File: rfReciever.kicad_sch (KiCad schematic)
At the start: 27 parts, among them P1 USB_C_Plug_USB2.0, SW1 SW_Push, SW2 SW_Push, U1 XBee_SMT, U2 CP2102N-Axx-xQFN20, U3 USBLC6-2SC6

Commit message: double schematic about to fix
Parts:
- removed U1: XBee_SMT, RF_Module:Digi_XBee_SMT, symbol RF_ZigBee:XBee_SMT
- added C1, C3: 4.7uF, Capacitor_SMD:C_0805_2012Metric, symbol Device:C
- added C2, C4: 0.1uF, Capacitor_SMD:C_0805_2012Metric, symbol Device:C
- added C5: 47pF, Capacitor_SMD:C_0805_2012Metric, symbol Device:C
- added C6: 1uF, Capacitor_SMD:C_0805_2012Metric, symbol Device:C
- added C7: 10uF, Capacitor_SMD:C_0805_2012Metric, symbol Device:C
- added D10, D5, D6, D7, D8, D9: LED, LED_SMD:LED_0805_2012Metric, symbol Device:LED
- added P2: USB_C_Plug_USB2.0, Connector_USB:USB_C_Plug_JAE_DX07P024AJ1, symbol Connector:USB_C_Plug_USB2.0
- added R1, R13, R14, R15, R16, R18, R19: 1K, Resistor_SMD:R_0805_2012Metric, symbol Device:R
- added R11: 10K, Resistor_SMD:R_0805_2012Metric, symbol Device:R
- added R12, R17: 10k, Resistor_SMD:R_0805_2012Metric, symbol Device:R
- added R4: 5.1K, Resistor_SMD:R_0805_2012Metric, symbol Device:R
- added SW3: SW_Push, Button_Switch_THT:SW_PUSH_6mm_H4.3mm, symbol Switch:SW_Push
- added U1: CP2102N-Axx-xQFN20, Audio_Module:QFN24_CP2102N_SIL, symbol Interface_USB:CP2102N-Axx-xQFN20
- added U4: USBLC6-2SC6, Package_TO_SOT_SMD:SOT-23-6, symbol Power_Protection:USBLC6-2SC6
- added X1, X2: DigiXBeeRX900Micro, symbol DataAcqLeaderBoard-Symbols:DigiXBeeRX900Micro
- C1, C3, C5: footprint Capacitor_SMD:C_0603_1608Metric_Pad1.08x0.95mm_HandSolder -> Capacitor_SMD:C_0805_2012Metric
- C2: footprint Capacitor_SMD:C_01005_0402Metric_Pad0.57x0.30mm_HandSolder -> Capacitor_SMD:C_0805_2012Metric
- C4, C6: footprint Capacitor_SMD:C_0402_1005Metric_Pad0.74x0.62mm_HandSolder -> Capacitor_SMD:C_0805_2012Metric
- C7: footprint Capacitor_SMD:C_0805_2012Metric_Pad1.18x1.45mm_HandSolder -> Capacitor_SMD:C_0805_2012Metric
- D1, D4: footprint LED_SMD:LED_0201_0603Metric -> LED_SMD:LED_0805_2012Metric
- D2, D3: footprint LED_SMD:LED_0603_1608Metric_Pad1.05x0.95mm_HandSolder -> LED_SMD:LED_0805_2012Metric
- R1, R10, R2, R3, R4, R9: footprint Resistor_SMD:R_0603_1608Metric_Pad0.98x0.95mm_HandSolder -> Resistor_SMD:R_0805_2012Metric
- R5, R8: value 330 -> 1K; footprint Resistor_SMD:R_0603_1608Metric_Pad0.98x0.95mm_HandSolder -> Resistor_SMD:R_0805_2012Metric
- R6, R7: value 220 -> 1K; footprint Resistor_SMD:R_0603_1608Metric_Pad0.98x0.95mm_HandSolder -> Resistor_SMD:R_0805_2012Metric
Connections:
- net 3.3V (out): now also X1.14 (SPI_N_SSEL/DIO17), X1.2 (VCC)
- net 5V(in): no longer R3.1
- net GND: now also C1.2, C2.2, C3.1, C4.1, C5.2, C6.2, C7.2, D10.1 (K), D5.1 (K), D6.1 (K), D7.1 (K), D8.1 (K), D9.1 (K), P2.A1 (GND), P2.A12 (GND), P2.B1 (GND), P2.B12 (GND), P2.S1 (SHIELD), R4.2, SW3.1, U1.12 (GND), U1.21 (GND), U1.3 (GND), U4.2 (GND), X1.1 (GND), X1.10 (GND), X1.12 (GND), X1.21 (GND), X1.32 (GND), X1.34 (GND), X2.1 (GND), X2.10 (GND), X2.12 (GND), X2.21 (GND), X2.32 (GND), X2.34 (GND)
- net at R2.1, R3.2: now also U1.8 (VBUS); no longer U2.8 (VBUS)
- net at R7.1, U2.18 (TXD): now also X1.4 (UART_RX/N_CONFIG/DIO14)
- net at R6.1, U2.17 (RXD): now also X1.3 (UART_TX/DIO13)
- net at R8.1: now also X1.7 (RSSI/PWM/DIO10)
- net at R5.1: now also X1.26 (ASSOCIATE/DIO5)
- net at U2.16 (~{RTS}): now also X1.24 (N_CTS/DIO7)
- net at U2.15 (~{CTS}): now also X1.27 (N_RTS/DIO6)
- new net: D6.2 (A), R14.2
- new net: C3.2, C4.2, R1.2, U1.6 (VDD)
- new net: P2.A5 (CC), R4.1
- new net: R19.1, X2.15 (ASSOCIATE/SPI_MOSI/DIO16)
- new net: D10.2 (A), R19.2
- new net: R12.2, SW3.2, X2.6 (N_RESET)
- new net: R11.2, X2.14 (SPI_N_SSEL/DIO17)
- new net: D5.2 (A), R13.2
- new net: R16.1, X2.25 (ON/N_SLEEP/DIO9)
- new net: R18.1, X2.26 (ASSOCIATE/DIO5)
- new net: R15.1, X2.7 (RSSI/PWM/DIO10)
- new net: D7.2 (A), R15.2
- new net: D8.2 (A), R16.2
- new net: D9.2 (A), R18.2
- new net: P2.A6 (D+), U4.3 (I/O2)
- new net: P2.A7 (D-), U4.1 (I/O1)
- new net: U1.4 (D+), U4.4 (I/O2)
- new net: U1.5 (D-), U4.6 (I/O1)
- new net 3.3V: C5.1, C6.1, C7.1, R1.1, R11.1, R12.1, R17.1, U1.9 (~{RST}), X2.2 (VCC)
- new net CTS(Bridge): U1.15 (~{CTS}), X2.27 (N_RTS/DIO6)
- new net RF_BOOTMODE: R17.2, X2.11 (N_BOOTMODE/SPI_N_ATTN/DIO19)
- new net RF_SLEEP: X2.9 (N_DTR/SLEEP_RQ/DIO8)
- new net RTS(Bridge): U1.16 (~{RTS}), X2.24 (N_CTS/DIO7)
- new net RXD(Bridge): R14.1, U1.17 (RXD), X2.3 (UART_TX/DIO13)
- new net TXD(Bridge): R13.1, U1.18 (TXD), X2.4 (UART_RX/N_CONFIG/DIO14)
- new net Vin(5V): C1.1, C2.1, P2.A4 (VBUS), P2.A9 (VBUS), P2.B4 (VBUS), P2.B9 (VBUS), R3.1, U1.7 (VREGIN), U4.5 (VBUS)
- no-connect marks 23 -> 36
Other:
- note removed: "Interface with external antenna if chosen"
- moved on the sheet: C1, C2, C3, C4, C5, C6, C7, D1, D2, D3, D4, P1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

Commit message: Final Schematic preliminary pcb layout(pre-routing)
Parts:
- removed C1, C3: 4.7uF, Capacitor_SMD:C_0805_2012Metric, symbol Device:C
- removed C2, C4: 0.1uF, Capacitor_SMD:C_0805_2012Metric, symbol Device:C
- removed C5: 1uF, Capacitor_SMD:C_0805_2012Metric, symbol Device:C
- removed C6: 47pF, Capacitor_SMD:C_0805_2012Metric, symbol Device:C
- removed C7: 10uF, Capacitor_SMD:C_0805_2012Metric, symbol Device:C
- removed D10, D3, D4, D5, D6: LED, LED_SMD:LED_0805_2012Metric, symbol Device:LED
- removed P1: USB_C_Plug_USB2.0, Connector_USB:USB_C_Plug_JAE_DX07P024AJ1, symbol Connector:USB_C_Plug_USB2.0
- removed R1, R13, R14, R19, R8: 1K, Resistor_SMD:R_0805_2012Metric, symbol Device:R
- removed R10, R9: 10k, Resistor_SMD:R_0805_2012Metric, symbol Device:R
- removed R4: 5.1K, Resistor_SMD:R_0805_2012Metric, symbol Device:R
- removed SW1, SW2, SW3: SW_Push, Button_Switch_THT:SW_PUSH_6mm_H4.3mm, symbol Switch:SW_Push
- removed U2: CP2102N-Axx-xQFN20, Audio_Module:QFN24_CP2102N_SIL, symbol Interface_USB:CP2102N-Axx-xQFN20
- removed U3: USBLC6-2SC6, Package_TO_SOT_SMD:SOT-23-6, symbol Power_Protection:USBLC6-2SC6
- removed X1, X2: DigiXBeeRX900Micro, symbol DataAcqLeaderBoard-Symbols:DigiXBeeRX900Micro
- added C8: 1u, Capacitor_SMD:C_0805_2012Metric, symbol Device:C
- added SW1: RF_RESET, Button_Switch_SMD:SW_SPST_CK_KMS2xxGP, symbol Switch:CK_KMS2xxG
- added X1: DigiXBeeRX900Micro, rfReciever-Footprints:XBeeXR900RFMicro, symbol xBeeRFSymbol:DigiXBeeRX900Micro
- R7: value 1K -> 1k; Link (none) -> https://www.mouser.com/ProductDetail/Vishay-Dale/CRCW08051K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; Mouser Part Number (none) -> 71-CRCW08051K00FKEAC; P/N (none) -> CRCW08051K00FKEAC
- U1: footprint Audio_Module:QFN24_CP2102N_SIL -> rfReciever-Footprints:QFN50P500X500X80-29N
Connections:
- net CTS(Bridge): now also X1.27 (N_RTS/DIO6)
- net GND: now also C8.2, SW1.2, SW1.SH (B), X1.1 (GND), X1.10 (GND), X1.12 (GND), X1.21 (GND), X1.32 (GND), X1.34 (GND)
- net RF_BOOTMODE: now also X1.11 (N_BOOTMODE/SPI_N_ATTN/DIO19)
- net RF_SLEEP: now also R16.1, X1.25 (ON/N_SLEEP/DIO9), X1.9 (N_DTR/SLEEP_RQ/DIO8)
- net RTS(Bridge): now also X1.24 (N_CTS/DIO7)
- net RXD(Bridge): now also R6.1, X1.3 (UART_TX/DIO13)
- net TXD(Bridge): now also R5.1, X1.4 (UART_RX/N_CONFIG/DIO14)
- net BRIDGE_VBUS: now reaches R2.1, R3.2, U1.8 (VBUS)
- net +3.3V: now reaches C3.2, C4.2, R1.2, U1.6 (VDD)
- net +3.3V: now also C5.1, C6.1, C7.1, R11.1, R12.1, R17.1, X1.2 (VCC)
- net BRIDGE_D1: now reaches D1.2 (A), R5.2
- net RF_RESET: now reaches R7.1
- net RF_RESET: now also R12.2, R7.2, C8.1, SW1.1, X1.6 (N_RESET)
- net BRIDGE_D2: now reaches D2.2 (A), R6.2
- net at R11.2: now also X1.14 (SPI_N_SSEL/DIO17)
- net RF_ASSOCIATE: now reaches R18.1
- net RF_ASSOCIATE: now also X1.26 (ASSOCIATE/DIO5)
- net RF_PWM: now reaches R15.1
- net RF_PWM: now also X1.7 (RSSI/PWM/DIO10)
- net RF_D7: now reaches D7.2 (A), R15.2
- net RF_D8: now reaches D8.2 (A), R16.2
- net RF_D9: now reaches D9.2 (A), R18.2
- net USB_IN_D+: now reaches P2.A6 (D+), U4.3 (I/O2)
- net USB_IN_D-: now reaches P2.A7 (D-), U4.1 (I/O1)
- net USB_D+: now reaches U1.4 (D+)
- net USB_D+: no longer U4.4 (I/O2)
- net USB_D-: now reaches U1.5 (D-)
- net USB_D-: no longer U4.6 (I/O1)
- removed net 3.3V: C5.1, C6.1, C7.1, R1.1, R11.1, R12.1, R17.1, U1.9 (~{RST})
- net Vin(5V) renamed +5V
- new net BRIDGE_3.3: R1.1, U1.9 (~{RST})
- new net USB_OUT_D+: U4.4 (I/O2)
- new net USB_OUT_D-: U4.6 (I/O1)
- no-connect marks 36 -> 19
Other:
- note added: "SI LABS USB-UART BRIDGE"
- note added: "USBC PLUG"
- note added: "XBeeRF MODULE MICRO"
- moved on the sheet: C1, C2, C3, C4, C5, C6, C7, D7, D8, D9, P2, R1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

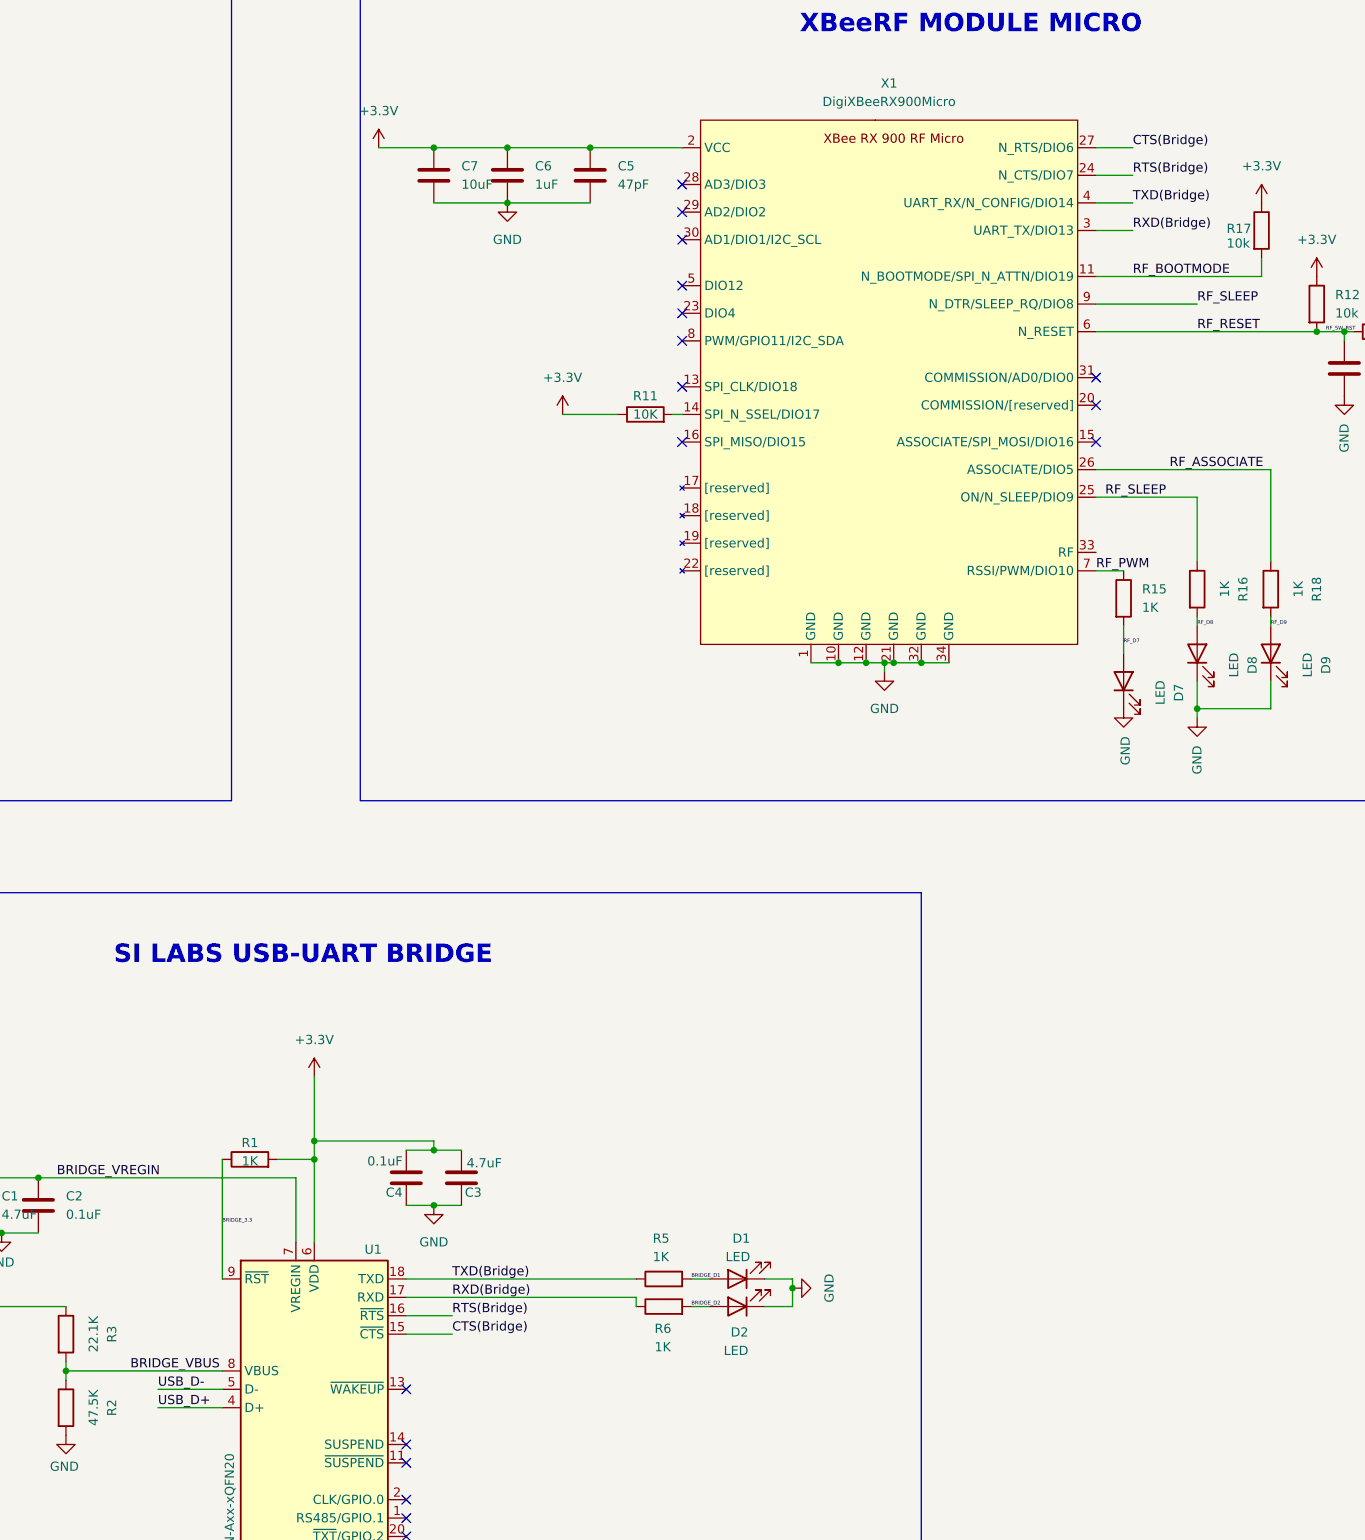
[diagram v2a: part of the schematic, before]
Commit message: Routing V1, possibly not DRC compliant
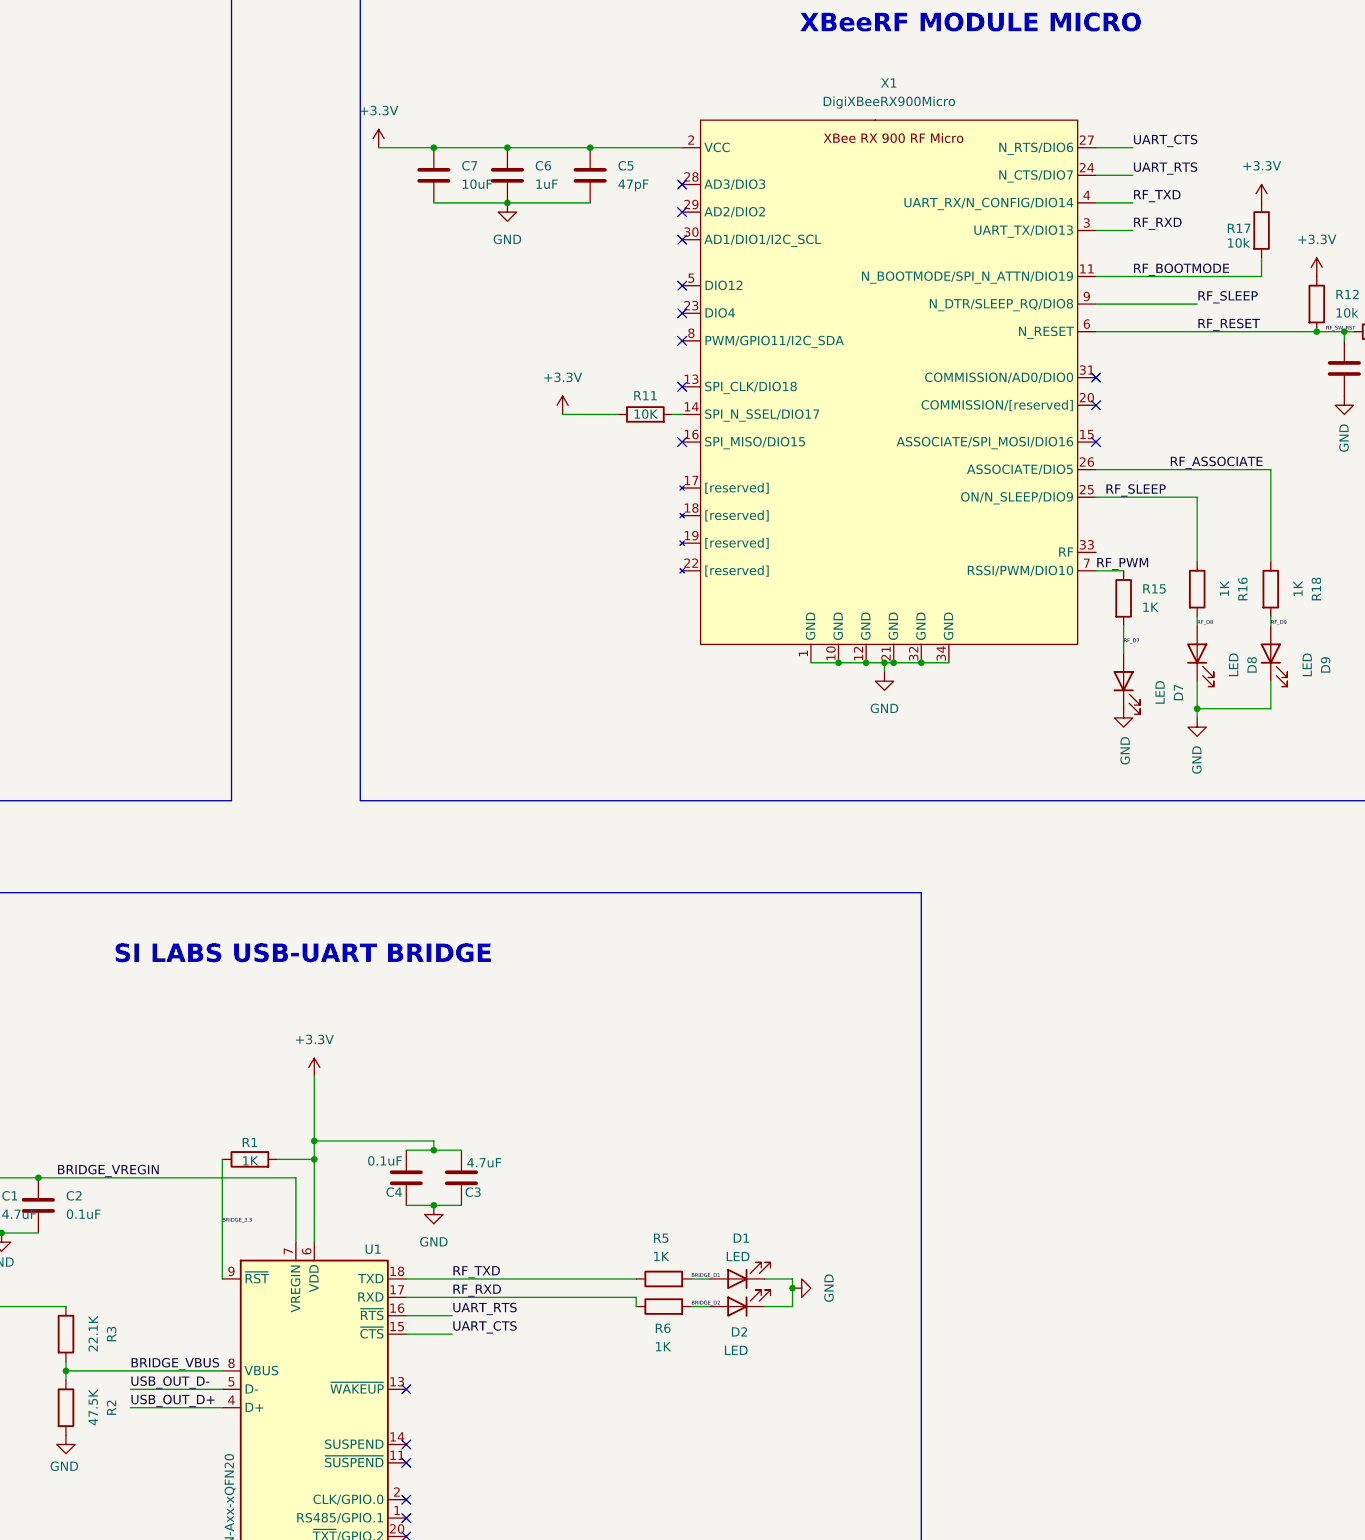
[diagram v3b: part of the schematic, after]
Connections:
- net USB_D+ is gone; now on net USB_OUT_D+: U1.4 (D+)
- net USB_D- is gone; now on net USB_OUT_D-: U1.5 (D-)
- net CTS(Bridge) renamed UART_CTS
- net RTS(Bridge) renamed UART_RTS
- net RXD(Bridge) renamed RF_RXD
- net TXD(Bridge) renamed RF_TXD
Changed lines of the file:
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@@
 	(wire
 		(pts
-			(xy 175.26 228.6) (xy 184.15 228.6)
+			(xy 171.45 228.6) (xy 184.15 228.6)
 		)
 		(stroke
@@
 	(wire
 		(pts
-			(xy 175.26 226.06) (xy 184.15 226.06)
+			(xy 171.45 226.06) (xy 184.15 226.06)
 		)
 		(stroke
@@
 		)
 	)
-	(label "TXD(Bridge)"
+	(label "RF_TXD"
 		(at 309.88 62.23 0)
 		(fields_autoplaced yes)
@@
 		)
 	)
-	(label "RTS(Bridge)"
+	(label "UART_RTS"
 		(at 215.9 215.9 0)
 		(fields_autoplaced yes)
@@
 		)
 	)
-	(label "RTS(Bridge)"
+	(label "UART_RTS"
 		(at 309.88 58.42 0)
 		(fields_autoplaced yes)
@@
 		)
 	)
-	(label "TXD(Bridge)"
+	(label "RF_TXD"
 		(at 215.9 210.82 0)
 		(fields_autoplaced yes)
@@
 		)
 	)
-	(label "USB_D+"
-		(at 175.26 228.6 0)
+	(label "USB_OUT_D+"
+		(at 171.45 228.6 0)
 		(fields_autoplaced yes)
 		(effects
@@
 		)
 	)
-	(label "CTS(Bridge)"
+	(label "UART_CTS"
 		(at 309.88 54.61 0)
 		(fields_autoplaced yes)
@@
 		)
 	)
-	(label "USB_D-"
-		(at 175.26 226.06 0)
+	(label "USB_OUT_D-"
+		(at 171.45 226.06 0)
 		(fields_autoplaced yes)
 		(effects
@@
 		)
 	)
-	(label "CTS(Bridge)"
+	(label "UART_CTS"
 		(at 215.9 218.44 0)
 		(fields_autoplaced yes)
@@
 		)
 	)
-	(label "RXD(Bridge)"
+	(label "RF_RXD"
 		(at 309.88 66.04 0)
 		(fields_autoplaced yes)
@@
 		)
 	)
-	(label "RXD(Bridge)"
+	(label "RF_RXD"
 		(at 215.9 213.36 0)
 		(fields_autoplaced yes)
